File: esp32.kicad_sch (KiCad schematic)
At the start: 21 parts, among them J2 TC2030-IDC, J3 Conn_01x04, J4 Conn_01x06, J5 USB_C_Receptacle_USB2.0, SW1 GT-TC029B-H025-L1N, SW2 GT-TC029B-H025-L1N, U3 RT9080-33GJ5, U4 ESP32-S3-WROOM-1

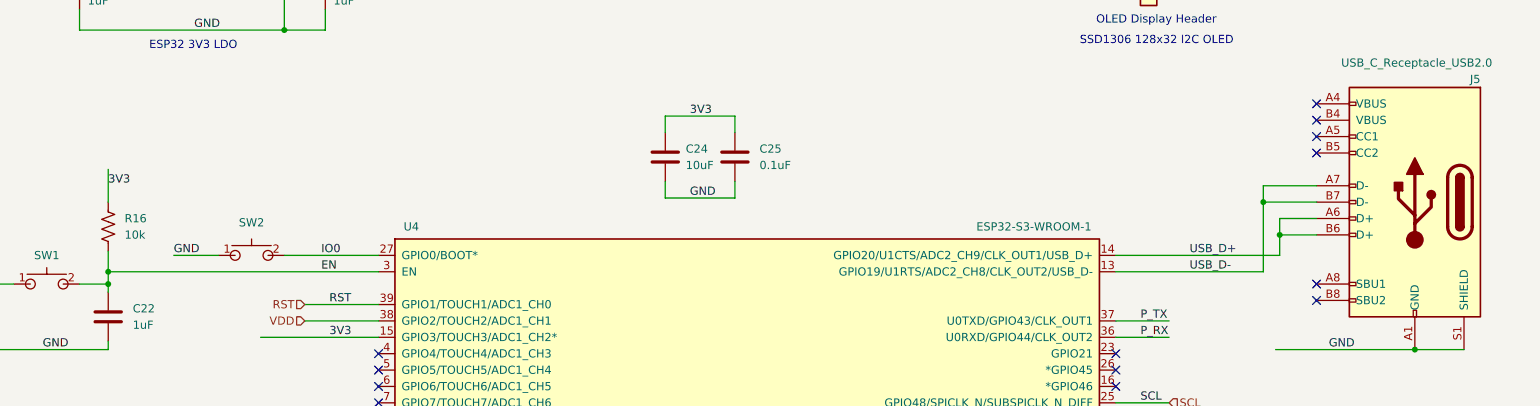
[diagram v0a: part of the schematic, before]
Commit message: eco-603-impl: schematic ECO (E0-E6, R2-R3)
E0 #6/8bd74c8: R21 removed, U9.8 to 1V2, U9.9 direct GND.
E1 #47: U2 SYNC/BCX_CLK/BCX_DAT to AGND.
E2 #25 + R2: R30-R32 4k7 PMBus, R35 10k PGD pull-ups.
E3 #13/#16: R22/R23 100R to 10R.
E4 #11/#17: F1 5A series, D1 SMAJ5.0A, C60 bulk.
E5 #37 + R3: R33/R34 5k1 CC, D2/D5 USB ESD, D3/D4 I2C ESD.
R3: C61 47u + C62 100n PVIN/AVIN bulk.
Rev 601->603. ERC: 18->19 err (PVIN PWR flag side effect of F1,
same benign class); netlist-verified, geometry-audited.
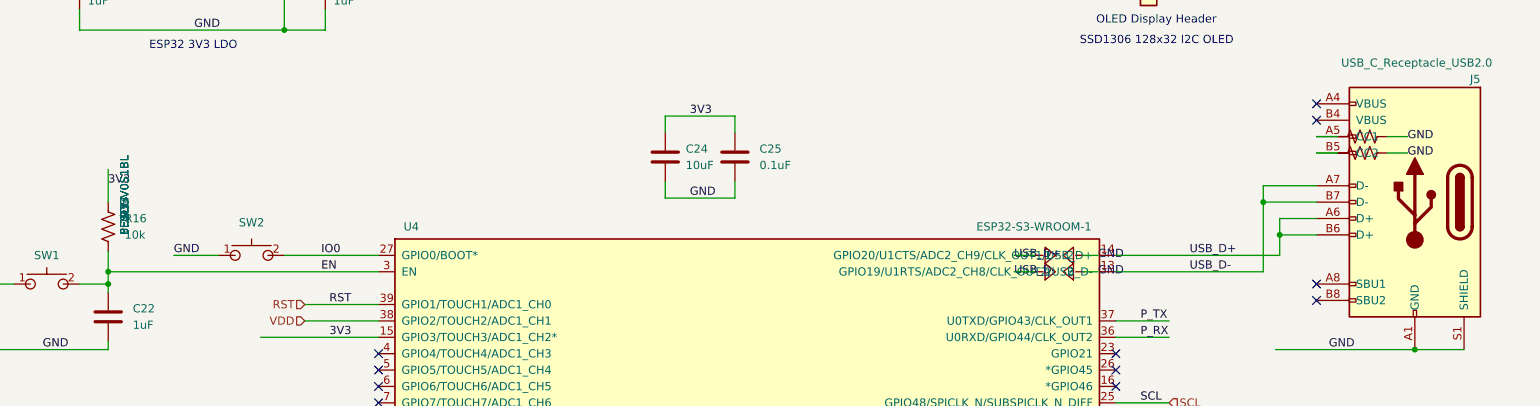
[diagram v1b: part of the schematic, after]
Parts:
- added D2, D5: PESD5V0S1BL, Diode_SMD:D_SOD-323, symbol bitaxe:TVS_BIDIR
- added R33, R34: 5.1k, Resistor_SMD:R_0402_1005Metric, symbol Device:R_US
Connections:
- net GND: now also D2.2, D5.2, R33.2, R34.2
- net USB_D+: now also D2.1
- net USB_D-: now also D5.1
- net at J5.A5 (CC1): now also R33.1
- net at J5.B5 (CC2): now also R34.1
- no-connect marks 24 -> 22
